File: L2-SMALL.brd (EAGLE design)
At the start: 8 parts

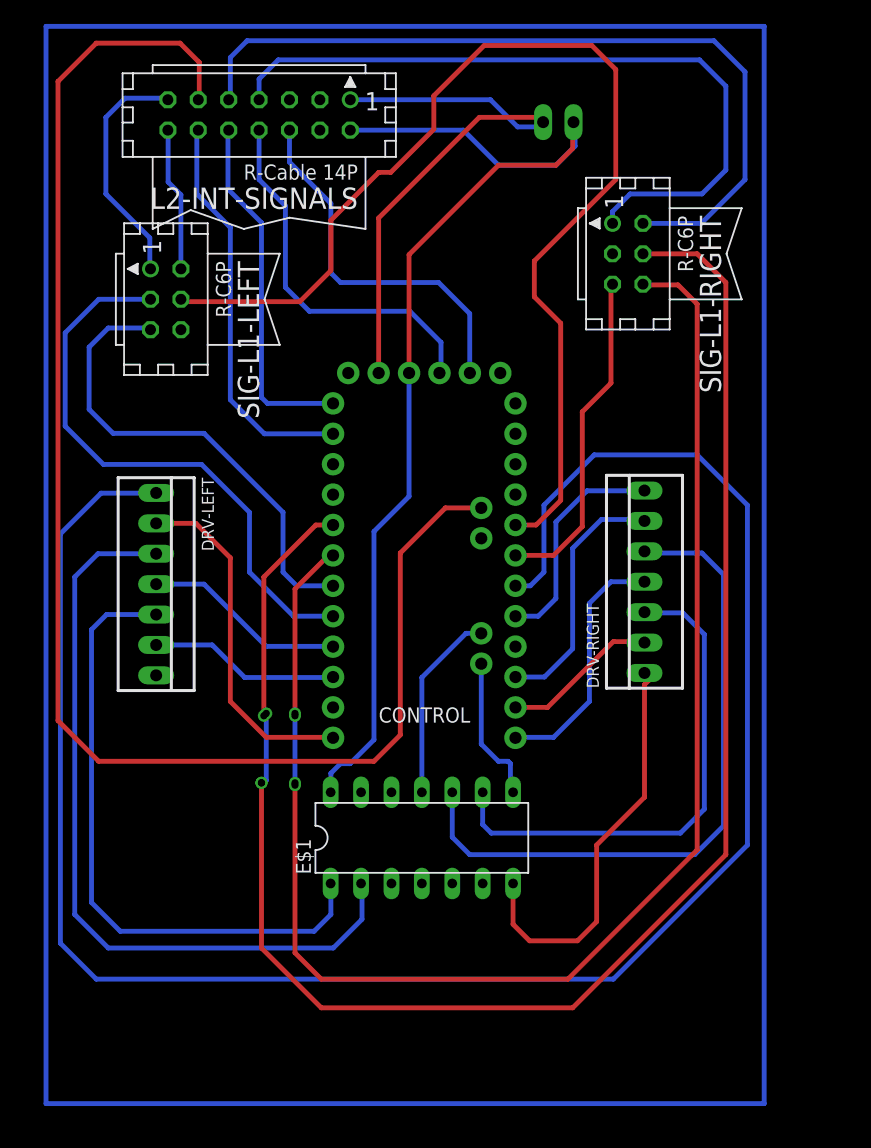
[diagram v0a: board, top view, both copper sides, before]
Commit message: redesigned all boards.
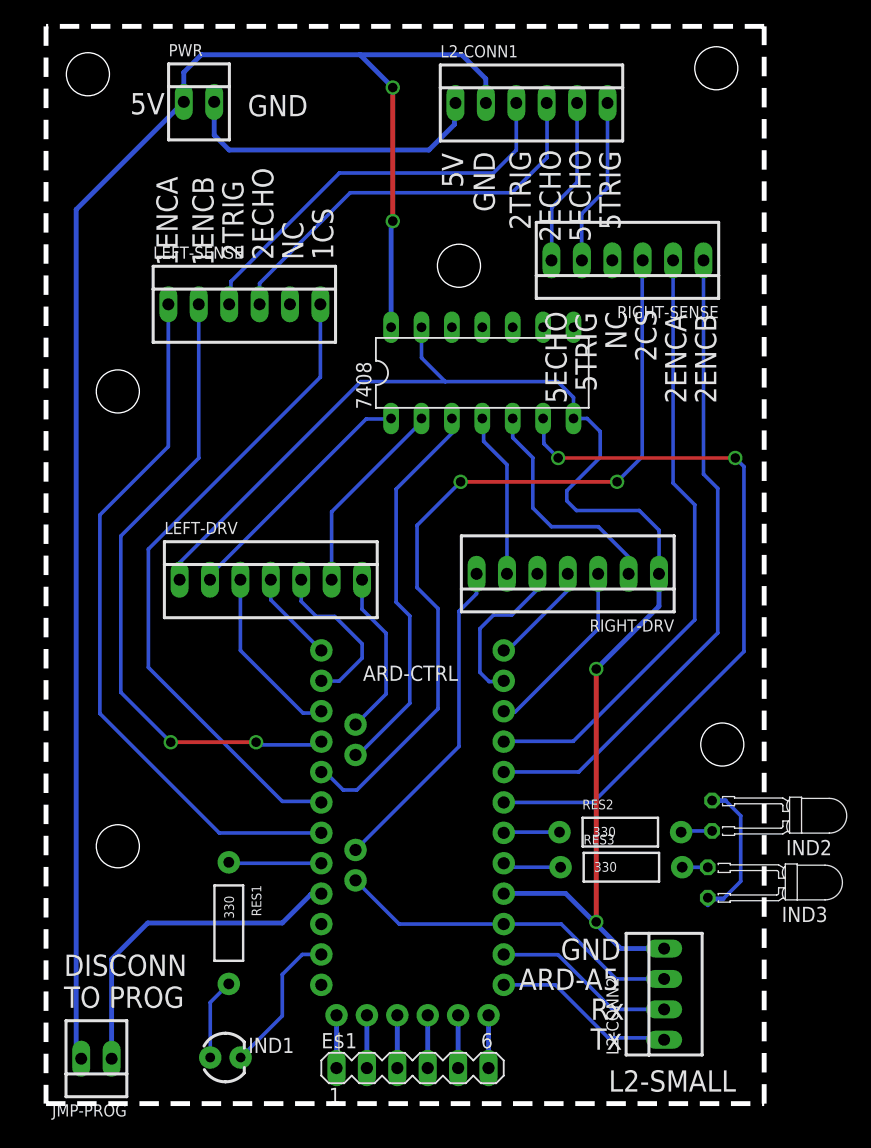
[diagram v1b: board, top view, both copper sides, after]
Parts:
- removed CONTROL: (no value), SparkFun-Boards:ARDUINO_PRO_MINI
- removed DRV-LEFT, DRV-RIGHT: (no value), con-molex:22-23-2071
- removed L2-INT-SIGNALS: (no value), con-harting:CON14
- removed SIG-L1-LEFT, SIG-L1-RIGHT: (no value), con-harting:CON06
- removed SUPPL-5V: (no value), con-molex:22-23-2021
- added 7408: (no value), 40xx:DIL14
- added ARD-CTRL: (no value), SparkFun-Boards:ARDUINO_PRO_MINI
- added IND1: (no value), SparkFun-LED:LED3MM
- added IND2, IND3: (no value), led:LED3MM_H7,5MM
- added JMP-PROG, PWR: (no value), con-molex:22-23-2021
- added L2-CONN1: female berg, con-molex:22-23-2061
- added L2-CONN2: female berg, con-molex:22-23-2041
- added LEFT-DRV, RIGHT-DRV: (no value), con-molex:22-23-2071
- added LEFT-SENSE, RIGHT-SENSE: (no value), con-molex:22-23-2061
- added RES1, RES2, RES3: 330, SparkFun-Passives:AXIAL-0.4
- E$1: device 74ttl-din:DIL14 -> con-lstb:MA06-1
- moved E$1 19.2 mm to (30.6, 2.97)
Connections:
- new net S$1: ARD-CTRL.A6, LEFT-DRV.7
- new net S$26: ARD-CTRL.GRN, E$1.1
- new net S$32: L2-CONN1.5, RIGHT-SENSE.6
- new net S$33: IND2.A, IND3.K
- new net S$34: ARD-CTRL.21, JMP-PROG.1
- new net S$40: ARD-CTRL.23, IND1.K
- new net S$41: ARD-CTRL.6, RES2.P$1
- new net S$42: ARD-CTRL.5, RES3.P$1
- new net S$43: IND2.K, RES2.P$2
- new net S$44: IND3.A, RES3.P$2
- new net S$45: 7408.13, 7408.7, ARD-CTRL.4, L2-CONN2.4, LEFT-DRV.1, RIGHT-DRV.1
- net S$10: now also ARD-CTRL.14, LEFT-DRV.5; no longer CONTROL.8, SIG-L1-LEFT.3
- net S$11: now also L2-CONN1.4, LEFT-SENSE.4; no longer CONTROL.15, DRV-RIGHT.6
- net S$12: now also 7408.1, LEFT-DRV.2; no longer CONTROL.14, DRV-RIGHT.2
- net S$13: now also 7408.2, LEFT-DRV.6; no longer CONTROL.13, DRV-RIGHT.4
- net S$14: now also 7408.4, RIGHT-DRV.6; no longer CONTROL.12, DRV-LEFT.2
- net S$15: now also 7408.5, RIGHT-DRV.2; no longer CONTROL.11
- net S$16: now also ARD-CTRL.15, LEFT-DRV.3; no longer CONTROL.10, DRV-LEFT.6
- net S$17: now also ARD-CTRL.19, LEFT-SENSE.1; no longer CONTROL.9, DRV-LEFT.4
- net S$18: now also ARD-CTRL.16, LEFT-SENSE.2; no longer CONTROL.7, SIG-L1-LEFT.5
- net S$19: now also ARD-CTRL.18, LEFT-SENSE.6; no longer L2-INT-SIGNALS.9, SIG-L1-RIGHT.2
- net S$2: now also 7408.14, JMP-PROG.2, L2-CONN1.2, PWR.1; no longer DRV-LEFT.3, E$1.2
- net S$20: now also ARD-CTRL.17, RIGHT-SENSE.3; no longer CONTROL.6, SIG-L1-RIGHT.6
- net S$21: now also ARD-CTRL.BLK, E$1.6; no longer CONTROL.5, SIG-L1-RIGHT.4
- net S$22: now also ARD-CTRL.GND, E$1.5; no longer L2-INT-SIGNALS.13, SIG-L1-LEFT.1
- net S$23: now also ARD-CTRL.VCC, E$1.4; no longer L2-INT-SIGNALS.14, SIG-L1-LEFT.2
- net S$24: now also ARD-CTRL.RXI, E$1.3; no longer CONTROL.A4
- net S$25: now also ARD-CTRL.TXO, E$1.2; no longer L2-INT-SIGNALS.7, SIG-L1-RIGHT.1
- net S$27: now also ARD-CTRL.A4, RIGHT-DRV.7; no longer CONTROL.A5, L2-INT-SIGNALS.11
- net S$28: now also ARD-CTRL.8, RIGHT-SENSE.1; no longer CONTROL.2, L2-INT-SIGNALS.12
- net S$29: now also L2-CONN1.1, PWR.2; no longer CONTROL.1, L2-INT-SIGNALS.10
- net S$3: now also ARD-CTRL.10, RIGHT-DRV.3; no longer CONTROL.GND, L2-INT-SIGNALS.1, SUPPL-5V.2
- net S$30: now also L2-CONN1.3, LEFT-SENSE.3; no longer CONTROL.A7, E$1.11
- net S$31: now also L2-CONN1.6, RIGHT-SENSE.5; no longer CONTROL.A6, E$1.8
- net S$35: now also ARD-CTRL.1, L2-CONN2.1; no longer DRV-RIGHT.5, E$1.10
- net S$36: now also ARD-CTRL.2, L2-CONN2.2; no longer DRV-RIGHT.3, E$1.9
- net S$37: now also ARD-CTRL.A5, L2-CONN2.3; no longer CONTROL.RXI, L2-INT-SIGNALS.8
- net S$38: now also ARD-CTRL.20, RES1.P$1; no longer CONTROL.TXO, L2-INT-SIGNALS.6
- net S$39: now also IND1.A, RES1.P$2; no longer DRV-RIGHT.1, E$1.7
- net S$4: now also ARD-CTRL.12, RIGHT-DRV.4; no longer CONTROL.VCC, E$1.14, L2-INT-SIGNALS.2, SUPPL-5V.1
- net S$5: now also ARD-CTRL.11, RIGHT-DRV.5; no longer DRV-LEFT.5, E$1.1
- net S$6: now also ARD-CTRL.9, RIGHT-SENSE.2; no longer CONTROL.20, SIG-L1-LEFT.4
- net S$7: now also 7408.3, ARD-CTRL.A7; no longer CONTROL.19, SIG-L1-RIGHT.5
- net S$8: now also ARD-CTRL.13, LEFT-DRV.4; no longer CONTROL.18, DRV-LEFT.1
- net S$9: now also 7408.6, ARD-CTRL.7; no longer CONTROL.17, DRV-RIGHT.7
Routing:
- net S$1: track 300.0 -> 14.0 mm
- net S$8: track 164.2 -> 7.66 mm
- net S$21: track 140.8 -> 4.41 mm, vias 2 -> 0
- net S$45: track 0.00 -> 117.0 mm, vias 0 -> 2
- net S$27: track 124.8 -> 27.3 mm
- net S$4: track 90.4 -> 8.81 mm
- net S$2: track 65.0 -> 139.0 mm, vias 0 -> 2
- net S$20: track 124.5 -> 66.8 mm
- net S$25: track 61.2 -> 4.41 mm
- net S$6: track 94.6 -> 51.0 mm
- net S$17: track 16.9 -> 59.3 mm
- net S$9: track 18.9 -> 60.4 mm, vias 0 -> 2
- net S$35: track 56.4 -> 15.3 mm
- net S$5: track 52.9 -> 13.4 mm
- net S$10: track 48.0 -> 13.8 mm
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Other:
- board outline added: 60 x 90 mm
- board text added: "1CS"
- board text added: "1ENCA"
- board text added: "1ENCB"
- board text added: "2CS"
- board text added: "2ECHO"
- board text added: "2ENCA"
- board text added: "2ENCB"
- board text added: "2TRIG"
- board text added: "5ECHO"
- board text added: "5TRIG"
- board text added: "5V"
- board text added: "ARD-A5"
- board text added: "DISCONN TO PROG"
- board text added: "GND"
- board text added: "L2-SMALL"
- board text added: "NC"
- board text added: "Rx"
- board text added: "Tx"
